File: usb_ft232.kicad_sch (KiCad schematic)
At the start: 0 parts

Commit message: [WIP] usb connector + ft232RNL
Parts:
- added C10, C6: 4.7uF, symbol Device:C_Polarized
- added C7, C9: 100nF, symbol Device:C
- added C8: 10nF, symbol Device:C
- added F1: Fuse, symbol Device:Fuse
- added L1: L_Ferrite, symbol Device:L_Ferrite
- added P1: 10164359-00011LF, Connector_USB:USB_C_Receptacle_GCT_USB4125-xx-x_6P_TopMnt_Horizontal, symbol Connector:USB_C_Plug_USB2.0
- added R5: 10k, symbol Device:R
- added U3: FT232RL, Package_SO:SSOP-28_5.3x10.2mm_P0.65mm, symbol Interface_USB:FT232RL
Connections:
- new net: C8.1, F1.2, L1.1
- new net CBUS3: U3.14 (CBUS3)
- new net FT232_RXD: U3.5 (RXD)
- new net FT232_TXD: U3.1 (TXD)
- new net GND: C10.2, C6.2, C7.2, C8.2, C9.2, P1.A1 (GND), P1.A12 (GND), P1.B1 (GND), P1.B12 (GND), U3.18 (GND), U3.21 (GND), U3.25 (AGND), U3.26 (TEST), U3.7 (GND)
- new net USBDM: P1.A7 (D-), U3.16 (USBD-)
- new net USBDP: P1.A6 (D+), U3.15 (USBD+)
- new net VBUS: C10.1, F1.1, P1.A4 (VBUS), P1.A9 (VBUS), P1.B4 (VBUS), P1.B9 (VBUS)
- new net VCC: C6.1, C7.1, L1.2
- new net VCC_IO: C9.1, R5.1, U3.17 (3V3OUT)
- new net shield: P1.S1 (SHIELD)
- new net ~DTR: U3.2 (DTR)
- new net ~EN_MIC2025: R5.2
- no-connect marks 0 -> 14

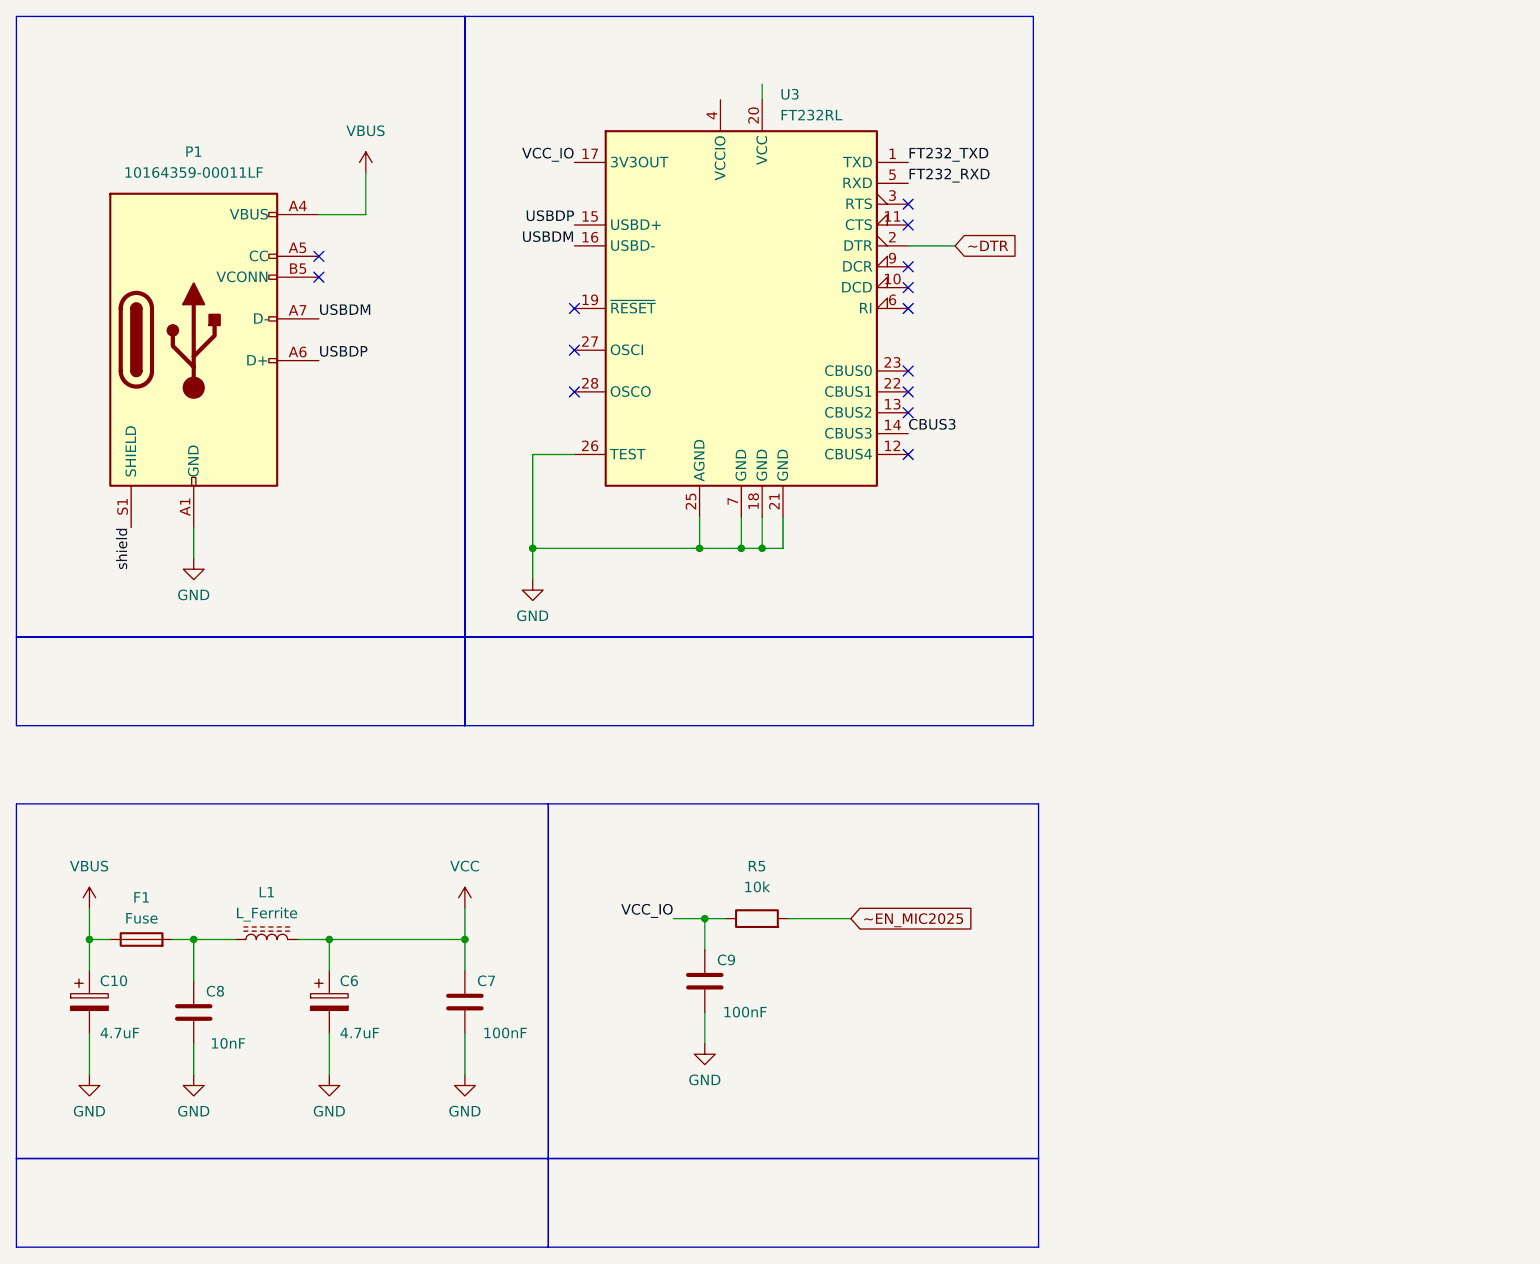
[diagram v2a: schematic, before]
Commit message: [ADD] comments and esd protection
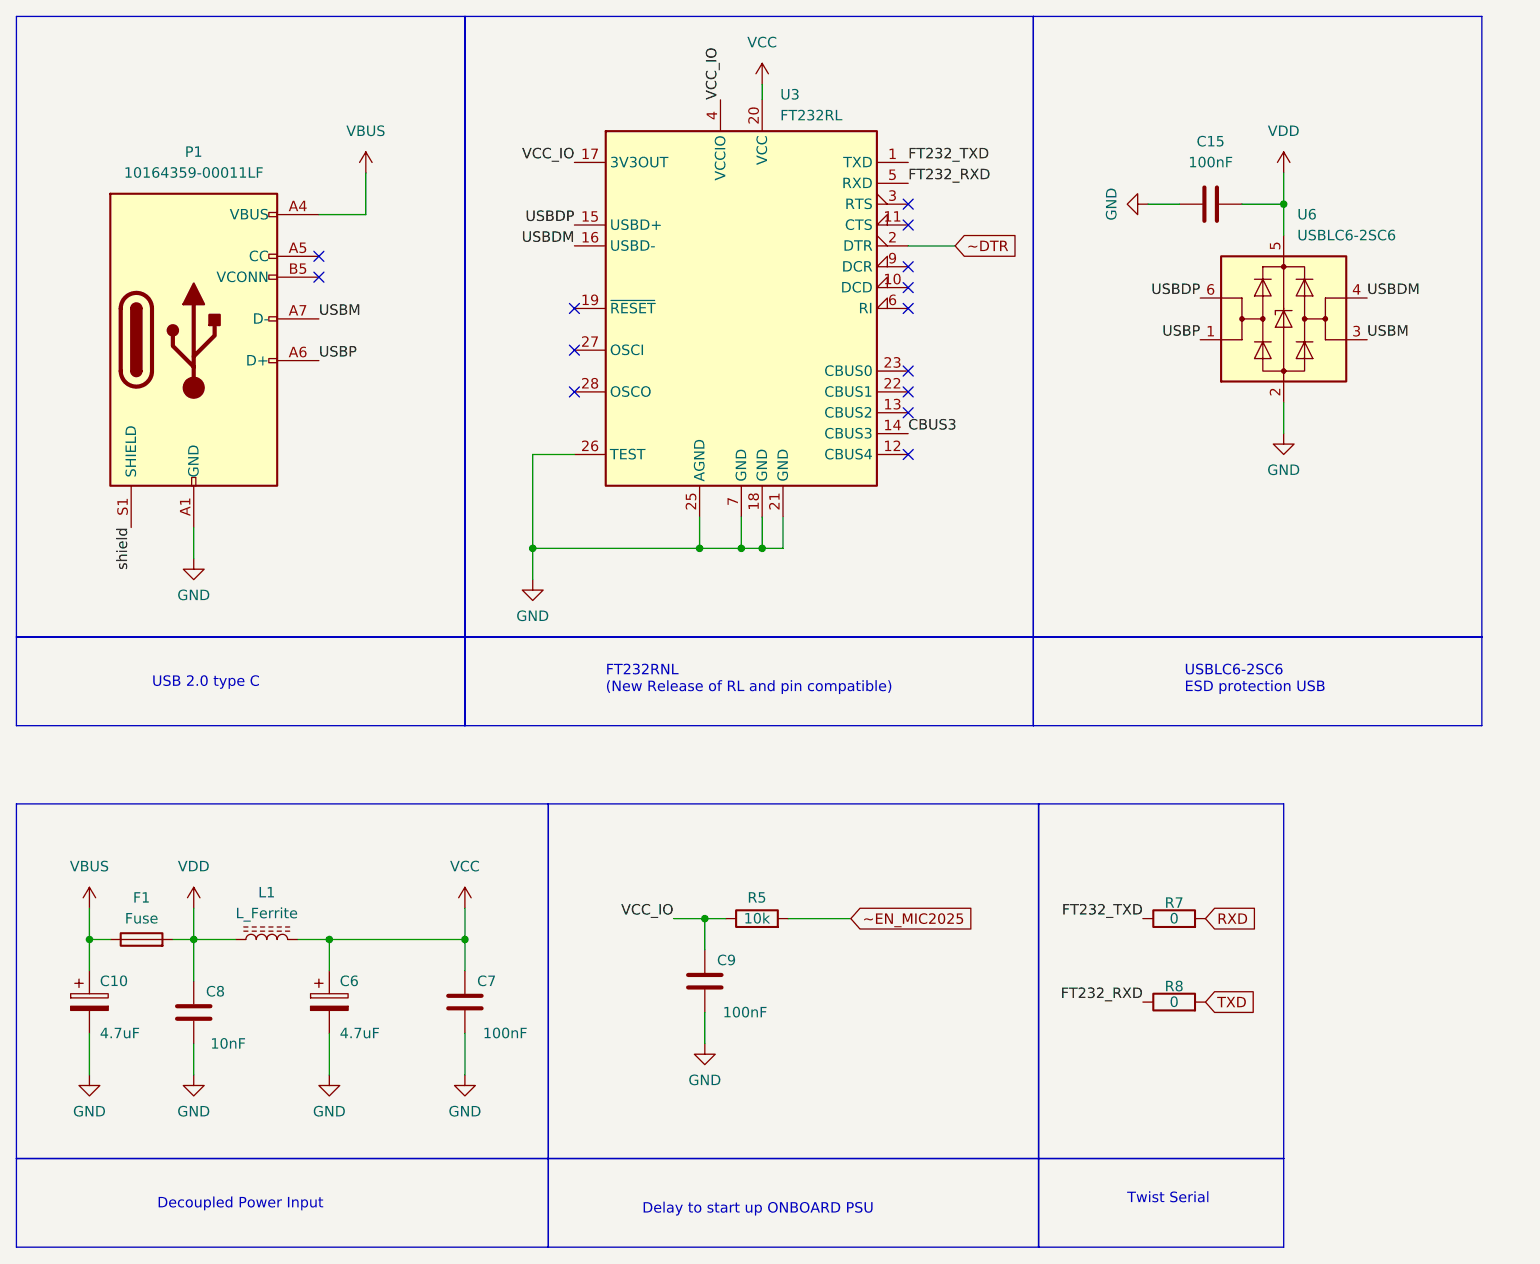
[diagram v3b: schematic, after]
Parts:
- added C15: 100nF, symbol Device:C
- added R7, R8: 0, symbol Device:R
- added U6: USBLC6-2SC6, Package_TO_SOT_SMD:SOT-23-6, symbol Power_Protection:USBLC6-2SC6
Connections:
- net FT232_RXD: now also R8.1
- net FT232_TXD: now also R7.1
- net GND: now also C15.1, U6.2 (GND)
- net USBDM: now also U6.4 (I/O2); no longer P1.A7 (D-)
- net USBDP: now also U6.6 (I/O1); no longer P1.A6 (D+)
- net VCC: now also U3.20 (VCC)
- net VCC_IO: now also U3.4 (VCCIO)
- net VDD: now reaches C8.1, F1.2, L1.1
- net VDD: now also C15.2, U6.5 (VBUS)
- new net RXD: R7.2
- new net TXD: R8.2
- new net USBM: P1.A7 (D-), U6.3 (I/O2)
- new net USBP: P1.A6 (D+), U6.1 (I/O1)
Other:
- note added: "Decoupled Power Input"
- note added: "Delay to start up ONBOARD PSU"
- note added: "FT232RNL (New Release of RL and pin compatible)"
- note added: "Twist Serial"
- note added: "USB 2.0 type C"
- note added: "USBLC6-2SC6 ESD protection USB"

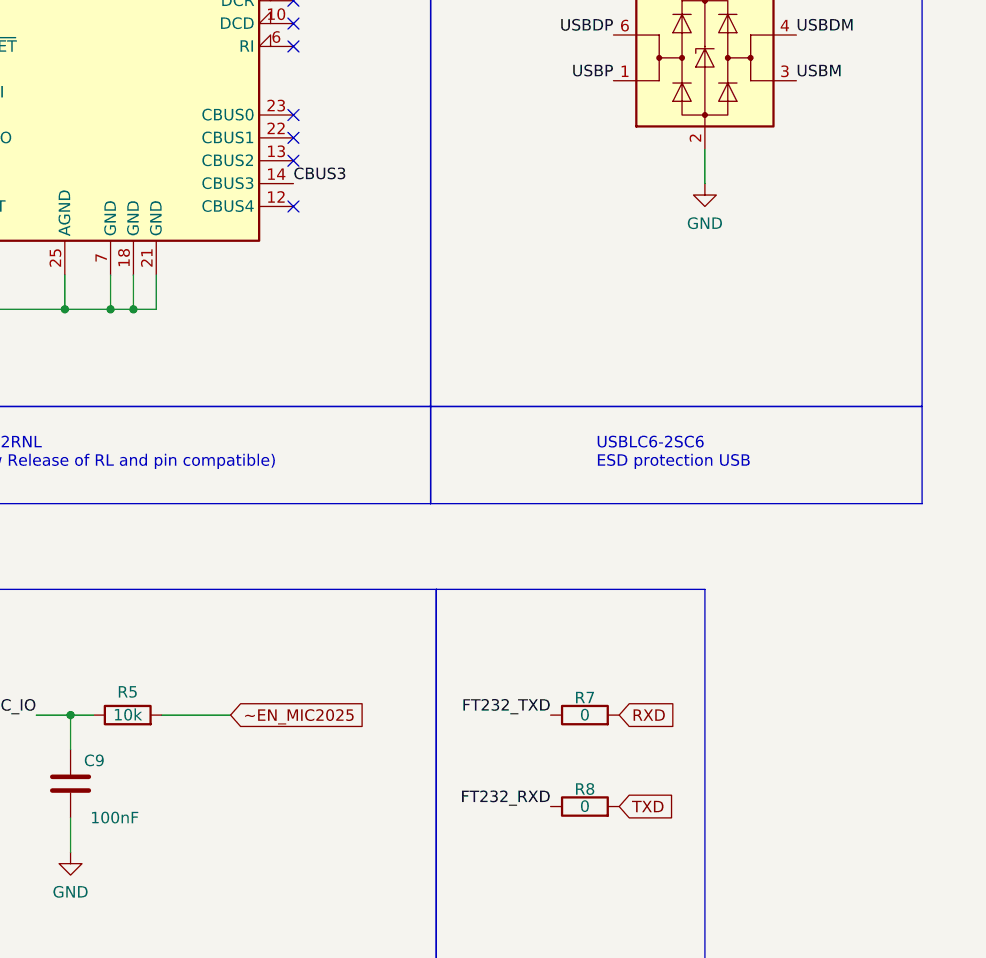
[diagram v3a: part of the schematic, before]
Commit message: [FIX] ERC failure, add sheets for output stage
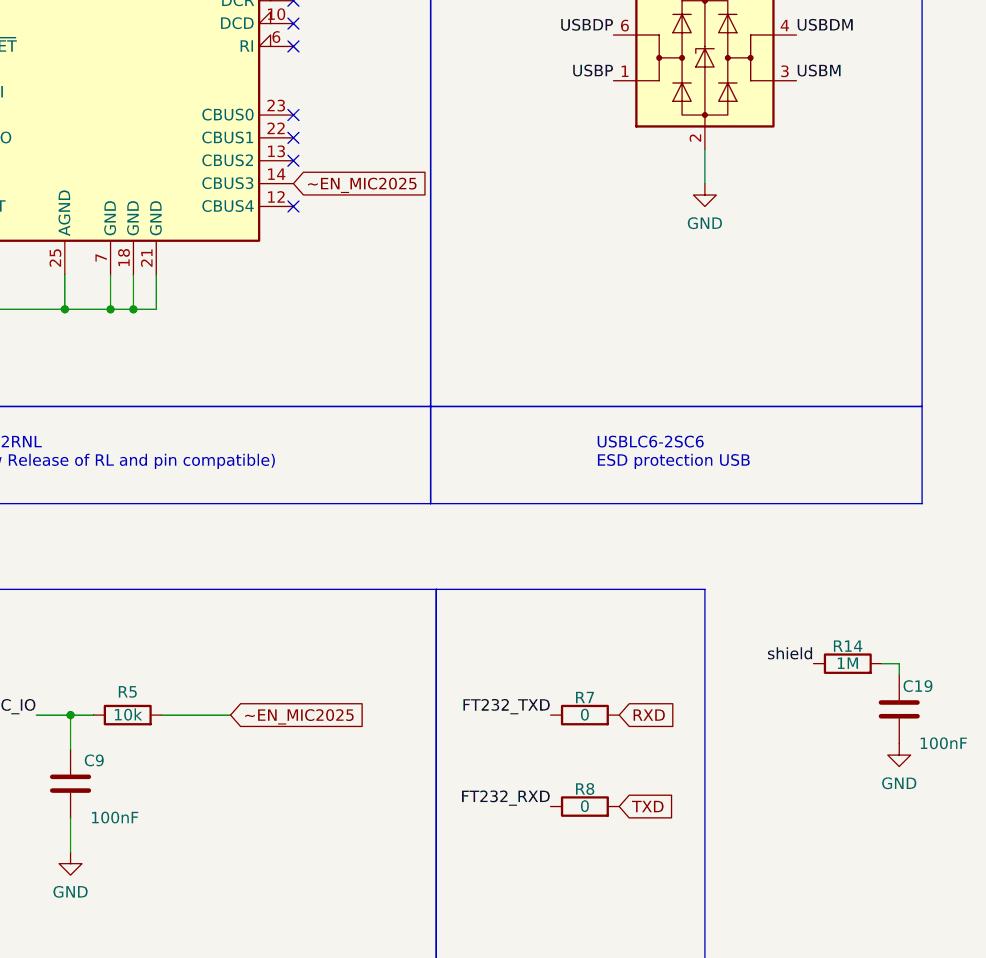
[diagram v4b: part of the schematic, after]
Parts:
- added C19: 100nF, symbol Device:C
- added R14: 1M, symbol Device:R
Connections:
- net CBUS3 is gone; now on net ~EN_MIC2025: U3.14 (CBUS3)
- net GND: now also C19.2
- net shield: now also R14.1
- new net: C19.1, R14.2
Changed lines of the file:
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@@
     (stroke (width 0) (type default))
   )
-  (wire (pts (xy 120.65 128.27) (xy 113.03 128.27))
+  (wire (pts (xy 113.03 128.27) (xy 120.65 128.27))
     (stroke (width 0) (type default))
   )
@@
     (stroke (width 0) (type default))
   )
+  (wire (pts (xy 194.945 122.555) (xy 194.945 123.825))
+    (stroke (width 0) (type default))
+  )
   (wire (pts (xy 40.64 127) (xy 40.64 130.81))
     (stroke (width 0) (type default))
   )
   (wire (pts (xy 109.855 83.185) (xy 112.395 83.185))
+    (stroke (width 0) (type default))
+  )
+  (wire (pts (xy 193.04 122.555) (xy 194.945 122.555))
     (stroke (width 0) (type default))
   )
@@
     (effects (font (size 1.27 1.27)) (justify left bottom))
   )
-  (label "CBUS3" (at 127.635 69.215 0) (fields_autoplaced)
-    (effects (font (size 1.27 1.27)) (justify left bottom))
+  (label "shield" (at 185.42 122.555 180) (fields_autoplaced)
+    (effects (font (size 1.27 1.27)) (justify right bottom))
   )
   (label "USBM" (at 183.515 57.785 0) (fields_autoplaced)
@@
     )
   )
+  (global_label "~EN_MIC2025" (shape input) (at 127.635 69.215 0) (fields_autoplaced)
+    (effects (font (size 1.27 1.27)) (justify left))
+    (property "Intersheetrefs" "${INTERSHEET_REFS}" (at 143.1386 69.215 0)
+      (effects (font (size 1.27 1.27)) (justify left) hide)
+    )
+  )
+  (symbol (lib_id "Device:R") (at 189.23 122.555 90) (unit 1)
+    (in_bom yes) (on_board yes) (dnp no)
+    (property "Reference" "R14" (at 189.23 120.65 90)
+      (effects (font (size 1.27 1.27)))
+    )
+    (property "Value" "1M" (at 189.23 122.555 90)
+      (effects (font (size 1.27 1.27)))
+    )
+    (property "Footprint" "" (at 189.23 124.333 90)
+      (effects (font (size 1.27 1.27)) hide)
+    )
+    (property "Datasheet" "~" (at 189.23 122.555 0)
+      (effects (font (size 1.27 1.27)) hide)
+    )
+    (pin "1")
+    (pin "2")
+    (instances
+      (project "JTAGFinder"
+        (path "/204d557f-3c83-43db-b1fd-628e15efe3d8/1bc3728f-429c-4b4e-ad94-277c4090b0e7"
+          (reference "R14") (unit 1)
+        )
+      )
+    )
+  )
   (symbol (lib_id "power:GND") (at 27.94 147.32 0) (unit 1)
     (in_bom yes) (on_board yes) (dnp no) (fields_autoplaced)
@@
         (path "/204d557f-3c83-43db-b1fd-628e15efe3d8/1bc3728f-429c-4b4e-ad94-277c4090b0e7"
           (reference "#PWR016") (unit 1)
+        )
+      )
+    )
+  )
+  (symbol (lib_id "Device:C") (at 194.945 127.635 0) (mirror y) (unit 1)
+    (in_bom yes) (on_board yes) (dnp no)
+    (property "Reference" "C19" (at 198.755 125.095 0)
+      (effects (font (size 1.27 1.27)) (justify left))
+    )
+    (property "Value" "100nF" (at 202.565 131.445 0)
+      (effects (font (size 1.27 1.27)) (justify left))
+    )
+    (property "Footprint" "" (at 193.9798 131.445 0)
+      (effects (font (size 1.27 1.27)) hide)
+    )
+    (property "Datasheet" "~" (at 194.945 127.635 0)
+      (effects (font (size 1.27 1.27)) hide)
+    )
+    (pin "1")
+    (pin "2")
+    (instances
+      (project "JTAGFinder"
+        (path "/204d557f-3c83-43db-b1fd-628e15efe3d8/1bc3728f-429c-4b4e-ad94-277c4090b0e7"
+          (reference "C19") (unit 1)
         )
       )
@@
         )
       )
+    )
+  )
+  (symbol (lib_id "power:GND") (at 194.945 131.445 0) (unit 1)
+    (in_bom yes) (on_board yes) (dnp no) (fields_autoplaced)
+    (property "Reference" "#PWR016" (at 194.945 137.795 0)
+      (effects (font (size 1.27 1.27)) hide)
+    )
+    (property "Value" "GND" (at 194.945 135.89 0)
+      (effects (font (size 1.27 1.27)))
+    )
+    (property "Footprint" "" (at 194.945 131.445 0)
+      (effects (font (size 1.27 1.27)) hide)
+    )
+    (property "Datasheet" "" (at 194.945 131.445 0)
+      (effects (font (size 1.27 1.27)) hide)
+    )
+    (pin "1")
+    (instances
+      (project "JTAGFinder"
+        (path "/204d557f-3c83-43db-b1fd-628e15efe3d8/651e631a-de0f-4a69-a119-5cdead14cfb1"
+          (reference "#PWR016") (unit 1)
+        )
+        (path "/204d557f-3c83-43db-b1fd-628e15efe3d8/1bc3728f-429c-4b4e-ad94-277c4090b0e7"
+          (reference "#PWR050") (unit 1)
+        )
+      )
